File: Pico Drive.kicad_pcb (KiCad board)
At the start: 2 copper layers, 100.3 x 102.2 mm, 31 parts, among them J1 Conn_01x06_Male, J2 Conn_01x08, J3 Conn_01x02_Male, J4 Conn_01x02_Male, SW1 Reset, U1 Pico, U2 74AXP1T45GWH, U3 74AHCT1G125, U4 OLED-I2C-Module-Aliexpress

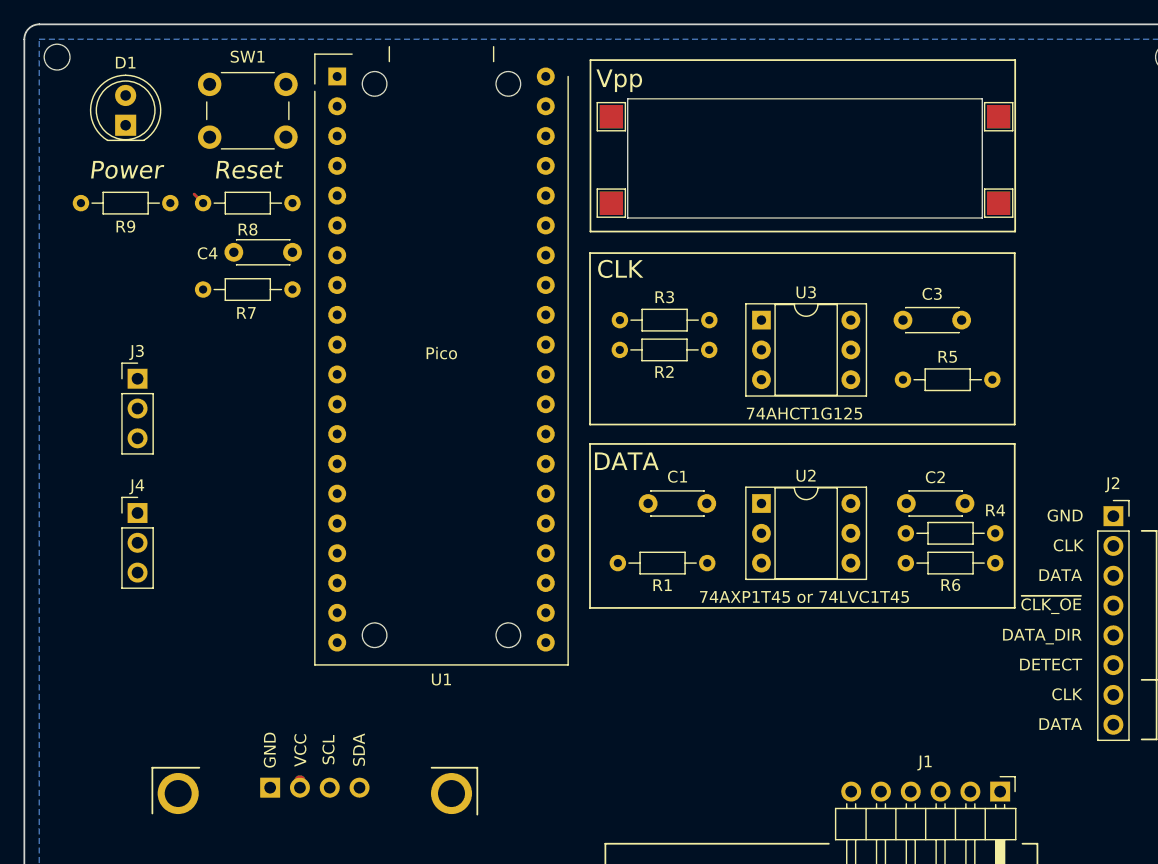
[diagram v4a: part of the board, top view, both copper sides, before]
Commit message: Swapped some TH for SMDs, fixed caps, tidied
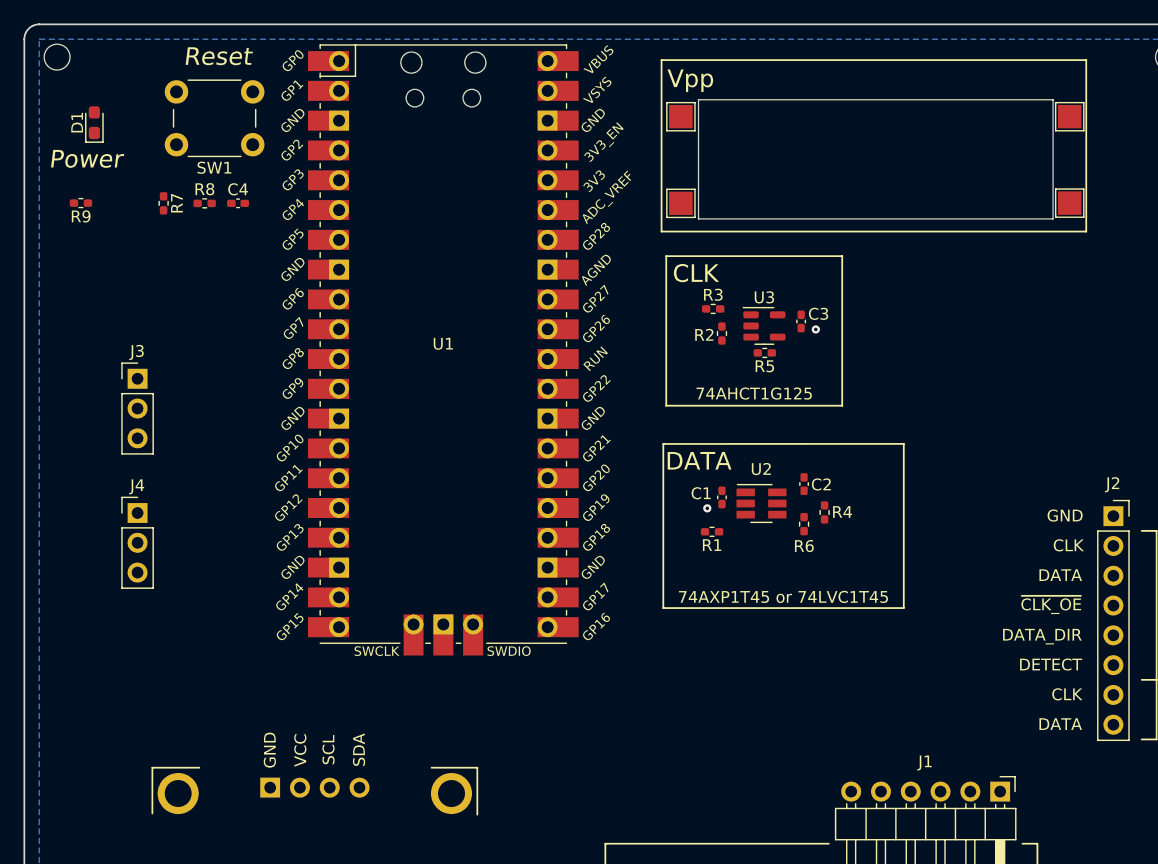
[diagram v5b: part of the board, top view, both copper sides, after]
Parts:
- C1, C2, C3: value 68nF -> 100n; footprint Capacitor_THT:C_Disc_D4.3mm_W1.9mm_P5.00mm -> Capacitor_SMD:C_0402_1005Metric_Pad0.74x0.62mm_HandSolder
- C4: value 100nF -> 100n; footprint Capacitor_THT:C_Disc_D4.3mm_W1.9mm_P5.00mm -> Capacitor_SMD:C_0402_1005Metric_Pad0.74x0.62mm_HandSolder
- D1: footprint LED_THT:LED_D5.0mm -> LED_SMD:LED_0603_1608Metric_Pad1.05x0.95mm_HandSolder
- R1, R2, R3, R4, R5, R6, R7, R8, R9: footprint Resistor_THT:R_Axial_DIN0204_L3.6mm_D1.6mm_P7.62mm_Horizontal -> Resistor_SMD:R_0402_1005Metric_Pad0.72x0.64mm_HandSolder
- SW1: footprint Button_Switch_THT:SW_PUSH_6mm_H4.3mm -> Button_Switch_THT:SW_PUSH_6mm
- U1: footprint kiwih_kicad:raspberrypi-pico-module -> RP-Pico Libraries:RPi_Pico_SMD_TH
- U2: footprint Package_DIP:DIP-6_W7.62mm_Socket -> Package_TO_SOT_SMD:SOT-23-6_Handsoldering
- U3: footprint Package_DIP:DIP-6_W7.62mm_Socket -> Package_TO_SOT_SMD:TSOT-23-5
- moved R7 13.2 mm to (29.7, 30.5), turned to -90 degrees
- moved R5 12.0 mm to (80.9, 43.2), turned to 180 degrees
- moved R6 9.29 mm to (84.2, 57.8), turned to -90 degrees
- moved C2 8.87 mm to (84.2, 54.4), turned to 90 degrees
- moved C3 8.68 mm to (84.0, 40.6), turned to -90 degrees
- moved R3 8.01 mm to (76.5, 39.5)
- moved R4 7.15 mm to (86.0, 56.8), turned to -90 degrees
- moved C4 6.24 mm to (36.0, 30.5), turned to 0 degrees
- moved REF** 6.06 mm to (106.9, 30.5)
- moved REF** 6.06 mm to (106.9, 23.1)
- moved REF** 5.93 mm to (73.8, 30.5)
- moved REF** 5.93 mm to (73.8, 23.1)
- moved SW1 2.90 mm to (37.2, 25.5)
- moved R1 2.70 mm to (76.4, 58.5)
- moved D1 2.67 mm to (23.8, 23.6)
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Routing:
- net Net-(R7-Pad2): track 1.08 -> 0.00 mm
- net +3V3: track 0.56 -> 0.00 mm
- net GND: vias 0 -> 2
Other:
- outline, holes or cut-outs redrawn

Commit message: Rotated and shrank the board, tidied stuff up
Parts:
- removed REF** (x4): TestPoint_Pad_2.0x2.0mm, TestPoint:TestPoint_Pad_2.0x2.0mm
- removed U4: OLED-I2C-Module-Aliexpress, kiwih_kicad:OLED-I2C-Module-Aliexpress
- added J6: I2C, Connector_PinSocket_2.54mm:PinSocket_1x04_P2.54mm_Vertical, F.Cu at (54.8, 20.5)
- SW1: footprint Button_Switch_THT:SW_PUSH_6mm -> digikey-footprints:Switch_Tactile_SMD_4.5x4.5mm_TL3315NF160Q
- moved J4 100.8 mm to (126.0, 36.0)
- moved C3 58.3 mm to (31.7, 66.2), turned to 180 degrees
- moved C4 57.9 mm to (47.2, -26.2)
- moved D1 57.9 mm to (35.0, -33.1)
- moved R7 57.9 mm to (40.9, -26.2)
- moved R8 57.9 mm to (44.4, -26.2)
- moved R9 57.9 mm to (33.9, -26.3)
- moved R5 56.8 mm to (29.0, 66.2)
- moved U3 54.5 mm to (31.2, 63.5), turned to -90 degrees
- moved J3 53.8 mm to (75.1, 20.5), turned to -90 degrees
- moved R2 50.3 mm to (30.8, 60.8), turned to 180 degrees
- moved R3 48.3 mm to (33.2, 60.8), turned to 180 degrees
- moved SW1 48.1 mm to (80.8, 46.0)
- moved R6 42.9 mm to (42.0, 65.2)
- moved R4 42.3 mm to (45.0, 67.3)
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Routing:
- net GND: track 0.00 -> 4.00 mm, vias 2 -> 5
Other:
- board size 100.3 x 102.2 mm -> 67.3 x 92.5 mm
- board text added: "I2C"
- board text added: "UART0"
- board text removed: "Vpp"

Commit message: Complete revamp, with routing.
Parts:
- J1: footprint Connector_PinHeader_2.54mm:PinHeader_1x06_P2.54mm_Horizontal -> Connector_PinHeader_2.54mm:PinHeader_1x06_P2.54mm_Vertical
- J2: value Conn_01x08 -> Conn_01x05; footprint Connector_PinSocket_2.54mm:PinSocket_1x08_P2.54mm_Vertical -> Connector_PinSocket_2.54mm:PinSocket_1x05_P2.54mm_Vertical
- J3: value Conn_01x02_Male -> Conn_01x03_Male
- J4: value Conn_01x02_Male -> Conn_01x06; footprint Connector_PinHeader_2.54mm:PinHeader_1x03_P2.54mm_Vertical -> Connector_PinSocket_2.54mm:PinSocket_1x06_P2.54mm_Vertical
- U3: value 74AHCT1G125 -> 74AHCT1G125DBVTG4
- moved H4 81.2 mm to (92.2, 24.0), turned to 90 degrees
- moved R7 78.8 mm to (55.8, 51.1), turned to 0 degrees
- moved H3 77.5 mm to (92.2, 74.8), turned to 90 degrees
- moved C4 77.1 mm to (53.8, 50.6), turned to -90 degrees
- moved R8 77.0 mm to (55.8, 49.9), turned to 180 degrees
- moved H1 63.8 mm to (18.5, 23.8), turned to 90 degrees
- moved D1 62.1 mm to (55.4, 25.5), turned to 0 degrees
- moved R9 57.7 mm to (55.4, 27.2), turned to 0 degrees
- moved J4 57.1 mm to (78.8, 68.1), turned to 180 degrees
- moved H2 56.8 mm to (18.5, 74.8), turned to 90 degrees
- moved J3 55.5 mm to (20.5, 30.2), turned to 0 degrees
- moved R5 42.7 mm to (71.5, 70.3), turned to -90 degrees
- moved J6 42.3 mm to (20.5, 45.2), turned to 0 degrees
- moved C3 39.8 mm to (71.5, 67.2), turned to 90 degrees
- moved U3 37.5 mm to (68.4, 68.8), turned to 0 degrees
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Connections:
- J1 pad 3: unconnected-(J1-Pad3) -> +5V
- J1 pad 4: unconnected-(J1-Pad4) -> /VDD
- J2 pad 3: /DATA_3V3 -> /~{CLK_OE}
- J2 pad 5: /~{CLK_OE} -> /DATA_3V3
- J4 pad 1: GND -> /CLK_5V
- J4 pad 2: /UART1_TX -> GND
- J4 pad 3: /UART1_RX -> +5V
- U1 pad 22: /DATA_3V3 -> /~{CLK_OE}
- U1 pad 25: /~{CLK_OE} -> /DATA_3V3
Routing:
- net +5V: track 0.05 -> 148.9 mm
- net +3V3: track 0.00 -> 140.5 mm
- net /DATA_DIR: track 0.00 -> 36.1 mm
- net /~{CLK_OE}: track 0.00 -> 31.0 mm
- net /CLK_3V3: track 0.00 -> 26.4 mm
- net /DATA_3V3: track 0.00 -> 26.0 mm
- net /DATA_5V: track 0.00 -> 22.8 mm
- net /CLK_5V: track 0.00 -> 21.9 mm
- net /UART0_RX: track 0.00 -> 12.9 mm
- net /UART0_TX: track 0.00 -> 12.4 mm
- net /VDD: track 0.00 -> 12.0 mm
- net /~{RUN}: track 0.00 -> 9.96 mm
- net /I2C1_SDA: track 0.00 -> 7.13 mm
- net /I2C1_SCL: track 0.00 -> 7.13 mm
- net Net-(R7-Pad2): track 0.00 -> 3.18 mm
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- added copper zone on F.Cu, net GND
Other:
- board size 67.3 x 92.5 mm -> 79.2 x 56.2 mm
- board text added: "DIR"
- board text added: "For Psion SIBO SSDs v0.0.1"
- board text added: "PsiDrive"
- board text added: "V_{BACKUP}"
- board text added: "V_{CC}"
- board text added: "V_{PP}"
- board text added: "~{OE}"
- board text removed: "DATA_DIR"
- board text removed: "DETECT"
- board text removed: "Pico Drive"
- board text removed: "Power"
- board text removed: "~{CLK_OE}"

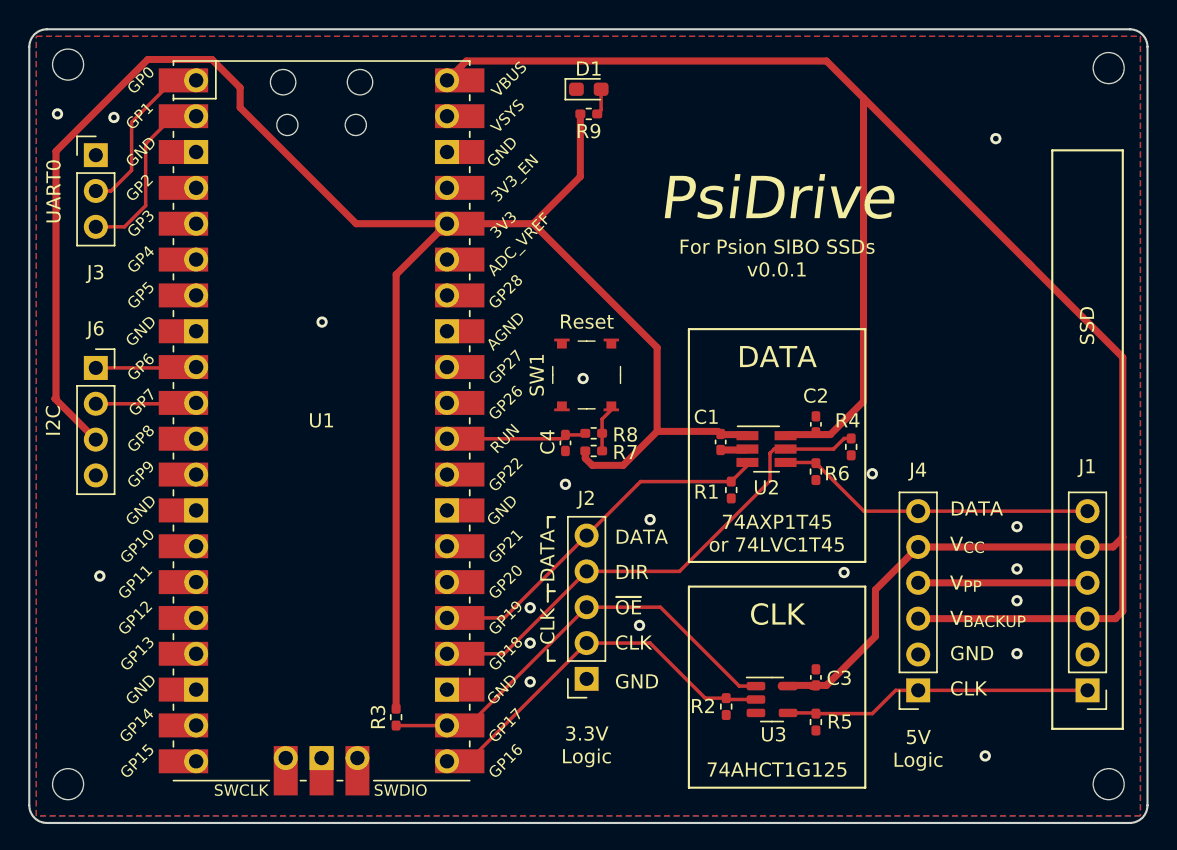
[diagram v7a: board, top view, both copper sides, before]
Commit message: Moved R3, changed U2 for SOT363, various fixes
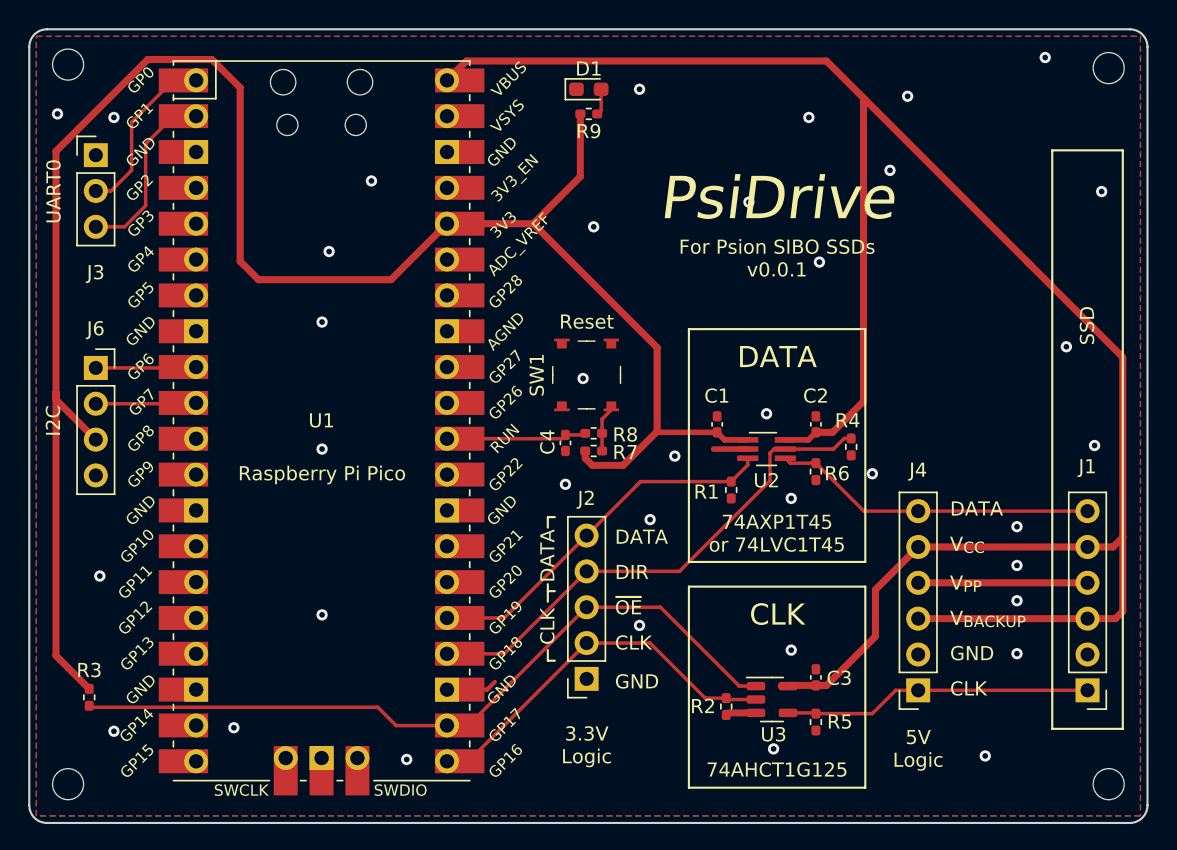
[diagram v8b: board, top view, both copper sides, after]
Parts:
- U2: footprint Package_TO_SOT_SMD:SOT-23-6_Handsoldering -> Package_TO_SOT_SMD:SOT-363_SC-70-6_Handsoldering
- moved R3 21.8 mm to (20.0, 68.6)
- moved C1 1.27 mm to (64.5, 49.2), turned to 90 degrees
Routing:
- net /~{CLK_OE}: track 31.0 -> 53.3 mm
- net GND: track 1.93 -> 8.21 mm, vias 19 -> 37
- net +3V3: track 140.5 -> 136.4 mm
- net /DATA_DIR: track 36.1 -> 36.9 mm
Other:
- board text added: "Raspberry Pi Pico"
